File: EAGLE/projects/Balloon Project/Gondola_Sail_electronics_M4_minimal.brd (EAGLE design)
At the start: 127 x 76.2 mm, 38 parts

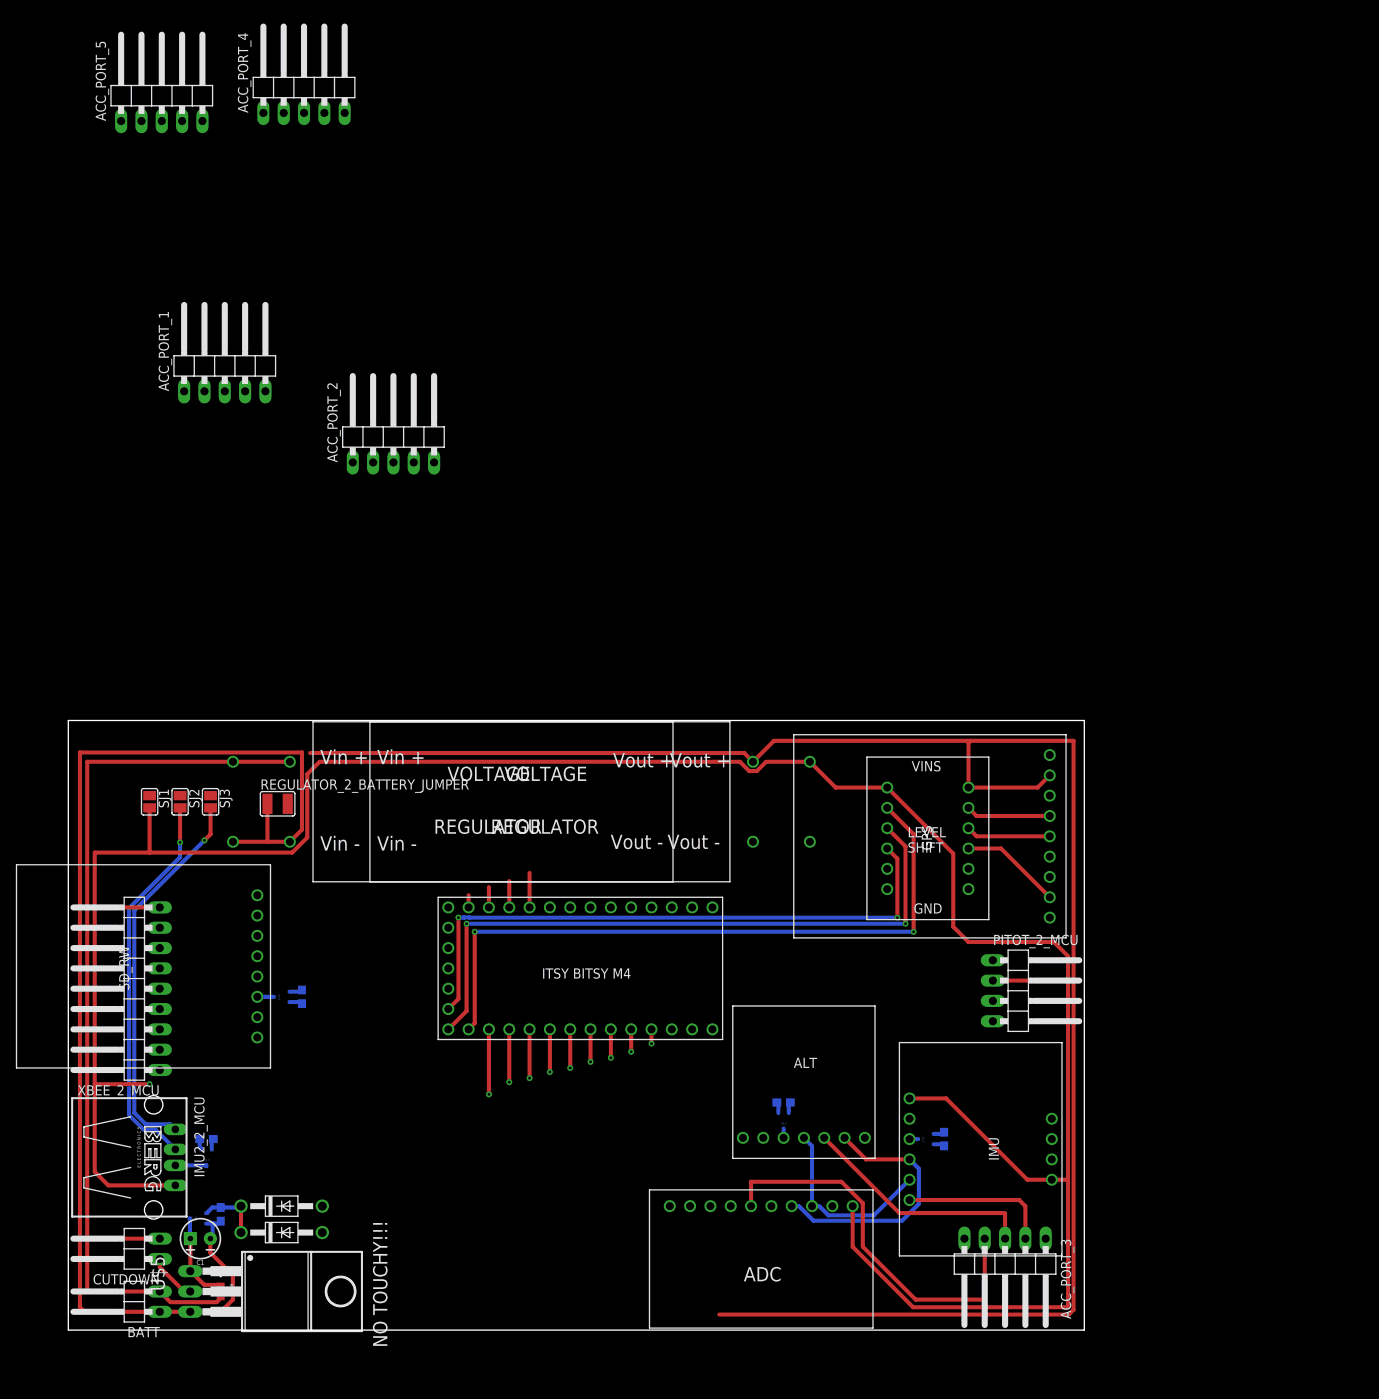
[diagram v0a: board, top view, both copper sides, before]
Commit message: added minimal sensorpack
full sensor pack has too many breakout pins, need to trim down the size of the board. starting routing traces
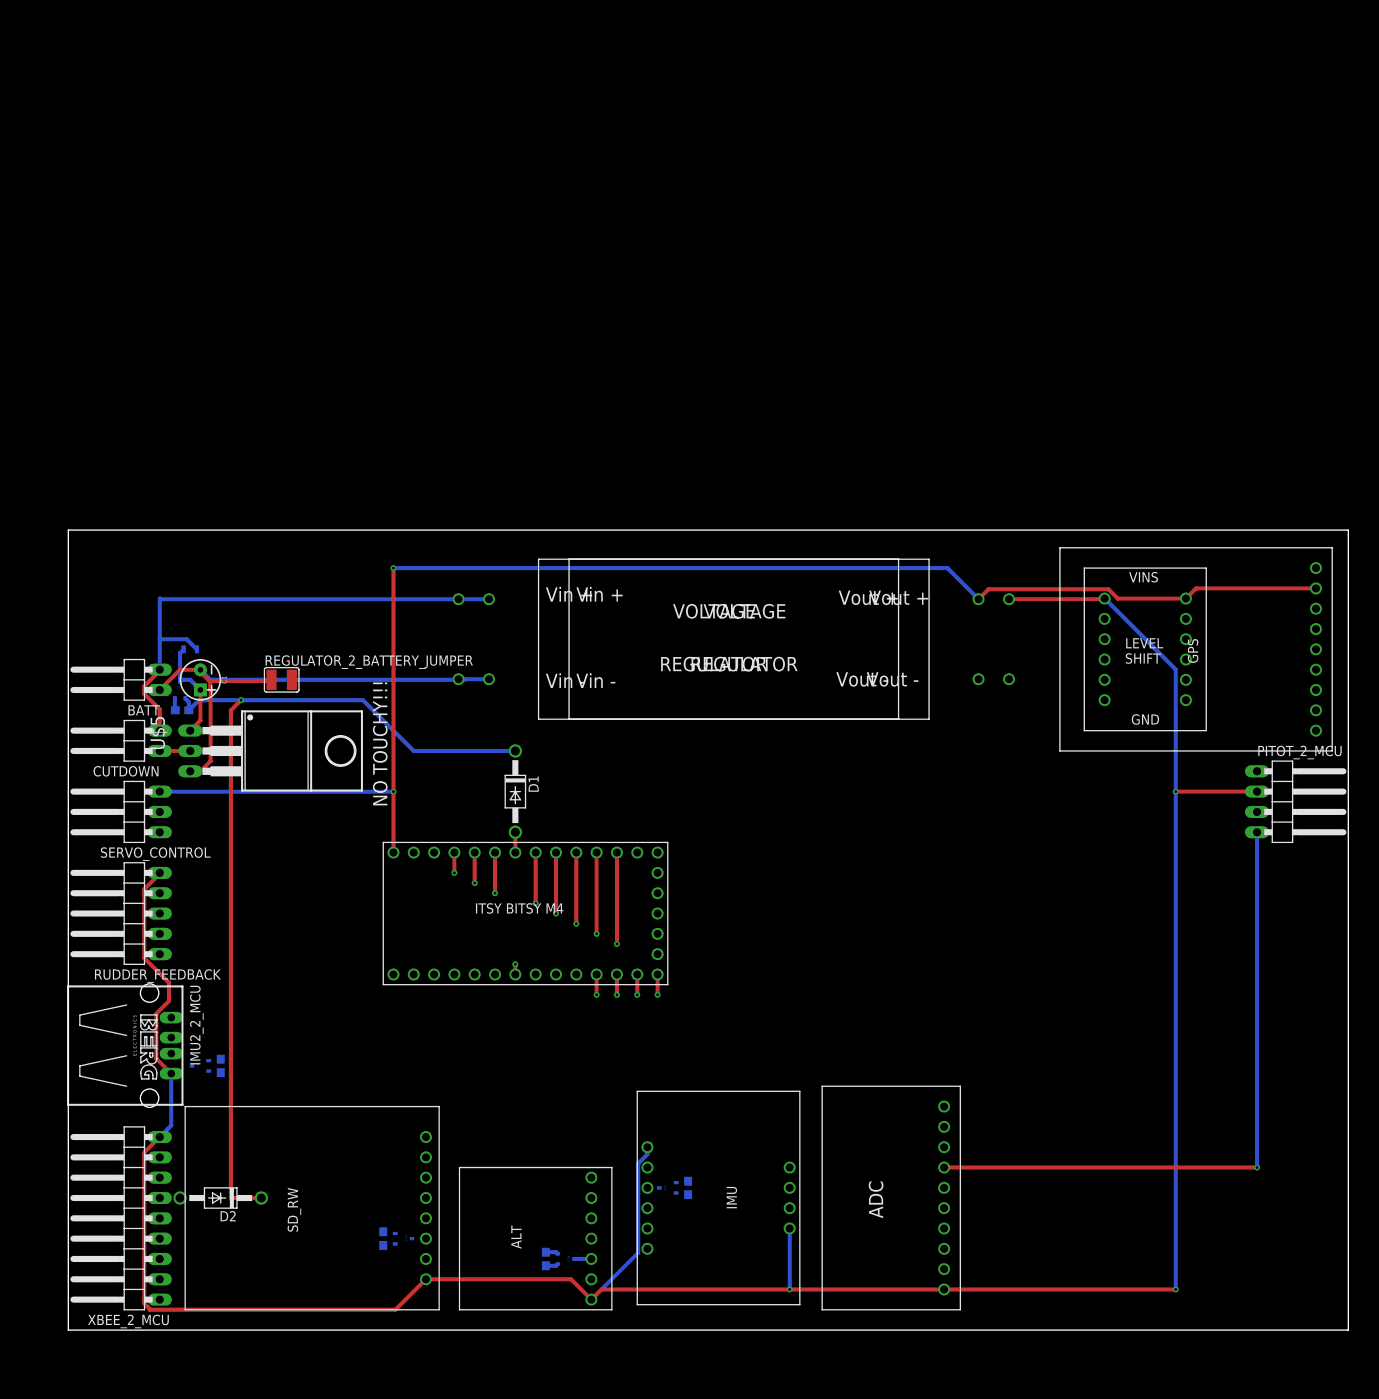
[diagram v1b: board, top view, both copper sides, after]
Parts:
- removed ACC_PORT_1, ACC_PORT_2, ACC_PORT_3, ACC_PORT_4, ACC_PORT_5: (no value), pinhead:1X05/90
- removed SJ1, SJ2, SJ3: (no value), jumper:SJ
- added RUDDER_FEEDBACK: (no value), pinhead:1X05/90
- added SERVO_CONTROL: (no value), pinhead:1X03/90
- moved R6 80.4 mm to (15.2, 85.1), flipped to the bottom, turned to 180 degrees
- moved BATT 77.7 mm to (7.62, 81.3)
- moved C1 69.8 mm to (16.5, 81.3), turned to 270 degrees
- moved U$5 67.6 mm to (26.7, 72.4)
- moved SD_POWER1 66.1 mm to (14.0, 80.0), turned to 0 degrees
- moved CUTDOWN 63.5 mm to (7.62, 73.7)
- moved R5 63.2 mm to (14.2, 77.5), turned to 0 degrees
- moved D1 62.4 mm to (55.9, 67.3), turned to 270 degrees
- moved U$1 40.7 mm to (141.0, 85.1)
- moved PITOT_2_MCU 40.6 mm to (152.4, 66.0)
- moved U$4 38.8 mm to (58.4, 11.4), turned to 90 degrees
- moved U$2 36.9 mm to (30.5, 15.2)
- moved U$6 36.0 mm to (134.6, 85.1)
- moved R2 35.6 mm to (59.7, 8.89), turned to 90 degrees
- moved 5V_REG 34.8 mm to (81.3, 86.4)
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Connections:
- removed net GPS_FIX_3V: ACC_PORT_2.2, U$6.A4
- removed net IMU_INT: ACC_PORT_3.1
- removed net RUDDER_SERVO_PWM: U$8.25
- new net RUDDER_SERVO_PWM_3V: U$6.A4, U$8.25
- new net RUDDER_SERVO_PWM_5V: SERVO_CONTROL.2, U$6.B4
- net 3V: now also RUDDER_FEEDBACK.5; no longer ACC_PORT_5.4, SJ1.2
- net 5V: now also SERVO_CONTROL.3; no longer ACC_PORT_5.5
- net ACC_MCU_A0: no longer ACC_PORT_2.5
- net ACC_MCU_A1: no longer ACC_PORT_2.4
- net ACC_MCU_A5: no longer ACC_PORT_2.3
- net ADC_ADDR: no longer SJ1.1, SJ2.1, SJ3.1
- net ADC_ALRT: no longer ACC_PORT_3.4
- net ALT_MISO: no longer ACC_PORT_3.3
- net GPS_FIX_5V: no longer ACC_PORT_2.1, U$6.B4
- net I2C_SCL: no longer ACC_PORT_1.2, SJ3.2
- net I2C_SDA: no longer ACC_PORT_1.1, SJ2.2
- net IMU1_PS0: no longer ACC_PORT_4.5
- net IMU1_PS1: no longer ACC_PORT_4.4
- net IMU1_RST: no longer ACC_PORT_3.2
- net LIMIT_SW_NEG: now also RUDDER_FEEDBACK.1
- net LIMIT_SW_POS: now also RUDDER_FEEDBACK.2
- net MCU_AREF: no longer ACC_PORT_4.2
- net MCU_EN: no longer ACC_PORT_4.1
- net MCU_RST: no longer ACC_PORT_4.3
- net MCU_SWCLK/RST: no longer ACC_PORT_5.1
- net MCU_SWDIO: no longer ACC_PORT_5.2
- net REG_GND: now also RUDDER_FEEDBACK.4, SERVO_CONTROL.1; no longer ACC_PORT_5.3
- net RUDDER_POT_VAR: now also RUDDER_FEEDBACK.3
- net SD_CD: no longer ACC_PORT_3.5
- net SPI_CLK: no longer ACC_PORT_1.5
- net SPI_MISO: no longer ACC_PORT_1.4
- net SPI_MOSI: no longer ACC_PORT_1.3
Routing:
- net CUTDOWN: track 8.54 -> 112.2 mm, vias 0 -> 1
- net BATT_GND: track 153.8 -> 68.0 mm
- net MCU_TX_3V: track 84.2 -> 0.00 mm, vias 2 -> 0
- net MCU_RX_3V: track 81.9 -> 0.00 mm, vias 2 -> 0
- net PITOT_VAR: track 0.00 -> 81.0 mm, vias 0 -> 1
- net I2C_SDA: track 89.5 -> 11.4 mm, vias 2 -> 1
- net GPS_EN_3V: track 76.0 -> 0.00 mm, vias 2 -> 0
- net I2C_SCL: track 78.1 -> 10.2 mm, vias 2 -> 1
- net BATT_VIN: track 118.1 -> 64.5 mm
- net ADC_ALRT: track 49.2 -> 0.00 mm
- net 5V: track 229.4 -> 183.2 mm, vias 0 -> 2
- net ALT_MISO: track 29.6 -> 0.00 mm
- net IMU1_RST: track 18.9 -> 0.00 mm
- net GPS_EN_5V: track 12.7 -> 0.00 mm
- net GPS_RX_5V: track 10.6 -> 0.00 mm
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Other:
- board size 127 x 76.2 mm -> 160 x 100 mm

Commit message: minimal telemetry/sensor board complete
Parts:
- added PITOT_OCS_JUMPER_OFF, PITOT_OCS_JUMPER_ON: (no value), jumper:SJ
- moved U$1 58.7 mm to (88.6, 58.4)
- moved U$6 58.7 mm to (82.3, 58.4)
- moved PITOT_2_MCU 54.9 mm to (104.4, 39.4)
- moved 3V_REG 17.3 mm to (67.8, 86.4)
- moved 5V_REG 17.3 mm to (64.0, 86.4)
- moved D1 8.14 mm to (47.8, 67.8)
- moved U$8 8.14 mm to (49.0, 52.6)
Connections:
- net 3V: now also PITOT_OCS_JUMPER_ON.1
- net PITOT_OCS: now also PITOT_OCS_JUMPER_OFF.2, PITOT_OCS_JUMPER_ON.2
- net REG_GND: now also PITOT_OCS_JUMPER_OFF.1
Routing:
- net I2C_SDA: track 11.4 -> 182.2 mm, vias 1 -> 5
- net I2C_SCL: track 10.2 -> 178.5 mm, vias 1 -> 5
- net RUDDER_POT_VAR: track 0.00 -> 121.3 mm, vias 0 -> 3
- net IMU1_PWR: track 3.81 -> 117.6 mm, vias 1 -> 5
- net RUDDER_SERVO_PWM_5V: track 0.00 -> 112.8 mm, vias 0 -> 3
- net ALT_PWR: track 6.65 -> 111.0 mm, vias 1 -> 5
- net SD_PWR: track 0.00 -> 90.5 mm, vias 0 -> 3
- net SPI_CLK: track 2.54 -> 89.8 mm, vias 1 -> 4
- net SPI_MISO: track 2.54 -> 87.6 mm, vias 1 -> 4
- net SPI_MOSI: track 2.54 -> 86.7 mm, vias 1 -> 4
- net XBEE_ATTN: track 7.62 -> 90.0 mm, vias 1 -> 3
- net XBEE_CS: track 8.89 -> 90.5 mm, vias 1 -> 3
- net XBEE_CMD: track 6.35 -> 80.0 mm, vias 1 -> 3
- net PITOT_VAR: track 81.0 -> 24.0 mm
- net RUDDER_SERVO_PWM_3V: track 0.00 -> 54.5 mm, vias 0 -> 2
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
